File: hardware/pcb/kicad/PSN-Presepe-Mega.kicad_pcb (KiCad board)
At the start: 2 copper layers, 280 x 170 mm, 83 parts, among them J1 12V_IN, K1 G5Q-1_DC12, K10 G5Q-1_DC12, K11 G5Q-1_DC12, K12 G5Q-1_DC12, K13 G5Q-1_DC12, K14 G5Q-1_DC12, K15 G5Q-1_DC12, K16 G5Q-1_DC12, K2 G5Q-1_DC12, K3 G5Q-1_DC12, K4 G5Q-1_DC12, K5 G5Q-1_DC12, K6 G5Q-1_DC12, K7 G5Q-1_DC12, K8 G5Q-1_DC12, K9 G5Q-1_DC12, Q1 IRLZ44N_CIELO_R, Q2 IRLZ44N_CIELO_G, Q3 IRLZ44N_CIELO_B, Q4 IRLZ44N_TRAM_R, Q5 IRLZ44N_TRAM_G, Q6 IRLZ44N_TRAM_B, Q7 IRLZ44N_ALBA_R, Q8 IRLZ44N_ALBA_G, Q9 IRLZ44N_ALBA_B, U1 ULN2803C, U2 ULN2803C

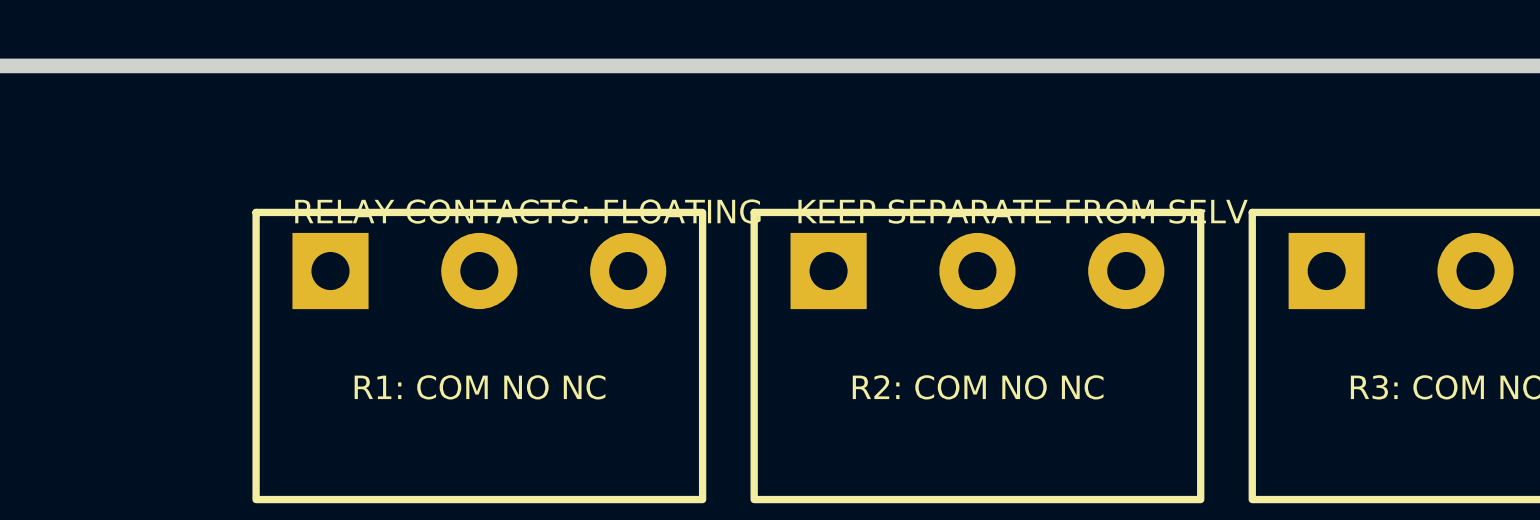
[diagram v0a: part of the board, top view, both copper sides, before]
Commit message: Remove redundant relay warning causing silk overlaps
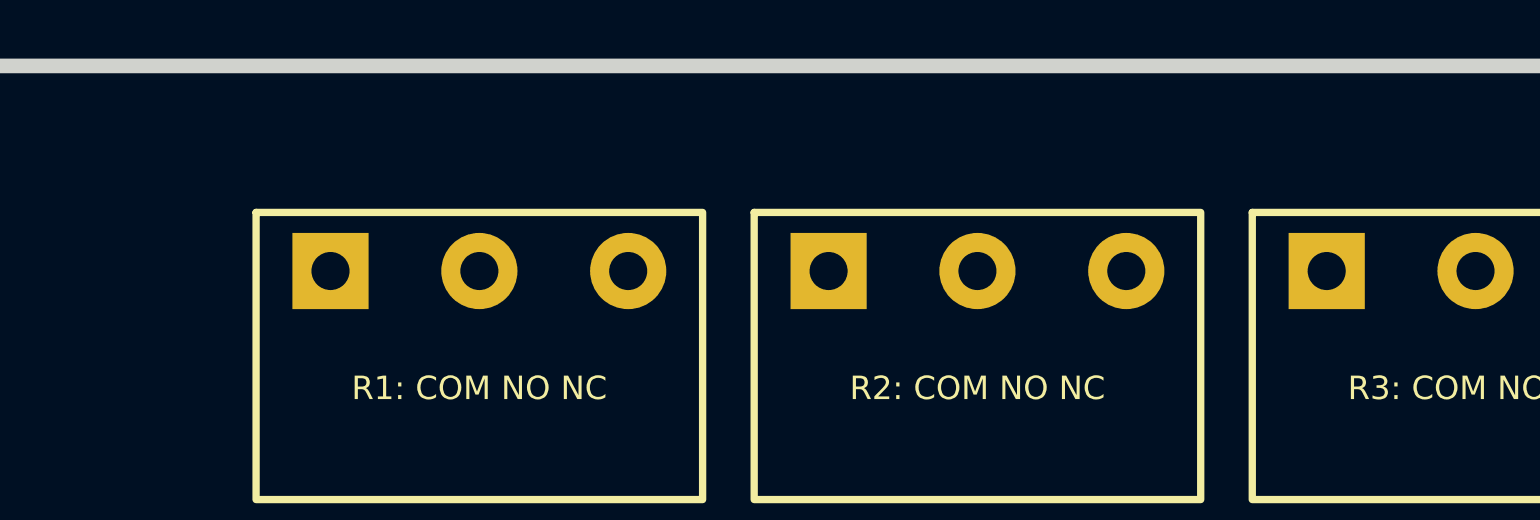
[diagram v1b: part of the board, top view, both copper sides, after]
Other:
- board text removed: "RELAY CONTACTS: FLOATING - KEEP SEPARATE FROM SELV"
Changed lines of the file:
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@@
   (gr_text "R15: COM NO NC" (at 286 149.08 90) (layer "F.SilkS") (effects (font (size 0.8 0.8) (thickness 0.12)) (justify)))
   (gr_text "R16: COM NO NC" (at 286 165.08 90) (layer "F.SilkS") (effects (font (size 0.8 0.8) (thickness 0.12)) (justify)))
-  (gr_text "RELAY CONTACTS: FLOATING - KEEP SEPARATE FROM SELV" (at 180 25) (layer "F.SilkS") (effects (font (size 0.8 0.8) (thickness 0.14))))
   (gr_text "NO GND PLANE UNDER CONTACT ROUTING" (at 100 35) (layer "F.SilkS") (effects (font (size 0.8 0.8) (thickness 0.12))))
   (footprint "MountingHole_1" (layer "F.Cu") (at 27 27)

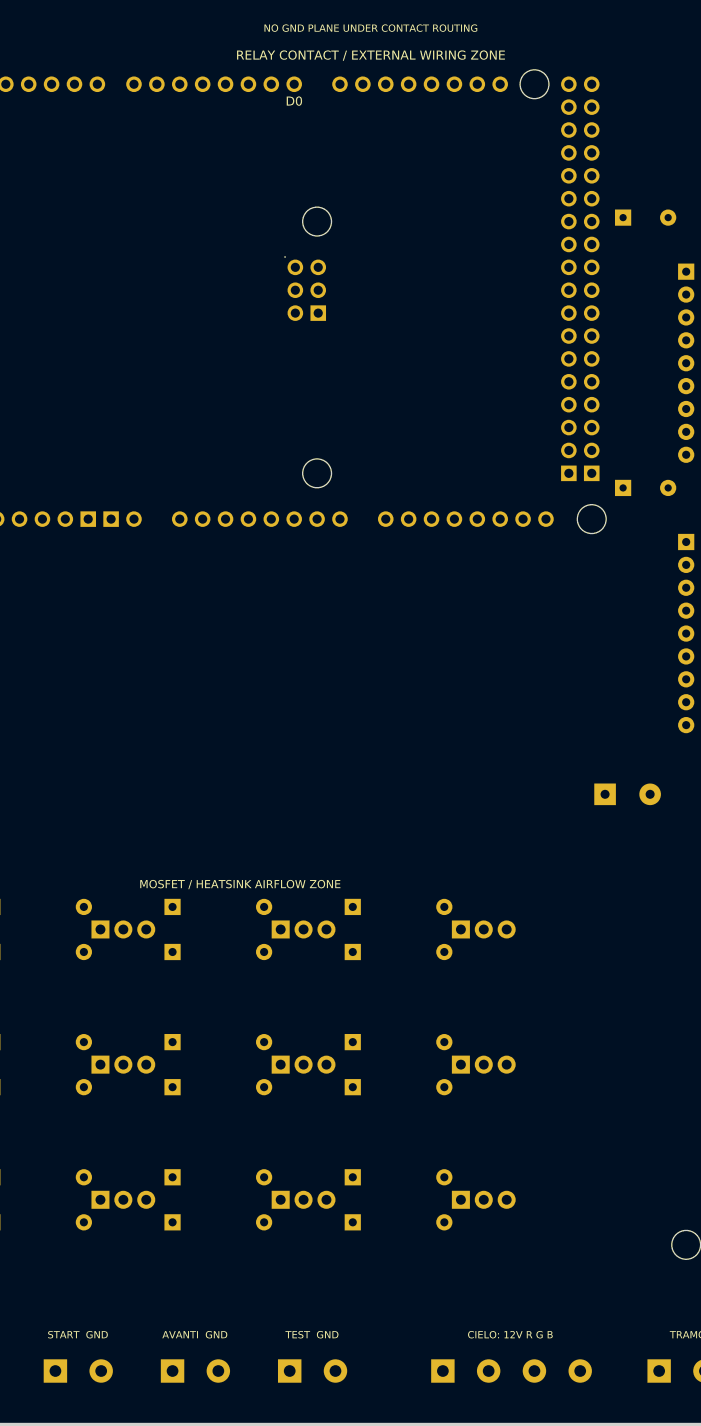
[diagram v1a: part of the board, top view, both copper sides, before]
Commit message: Promote first DRC-approved button routes
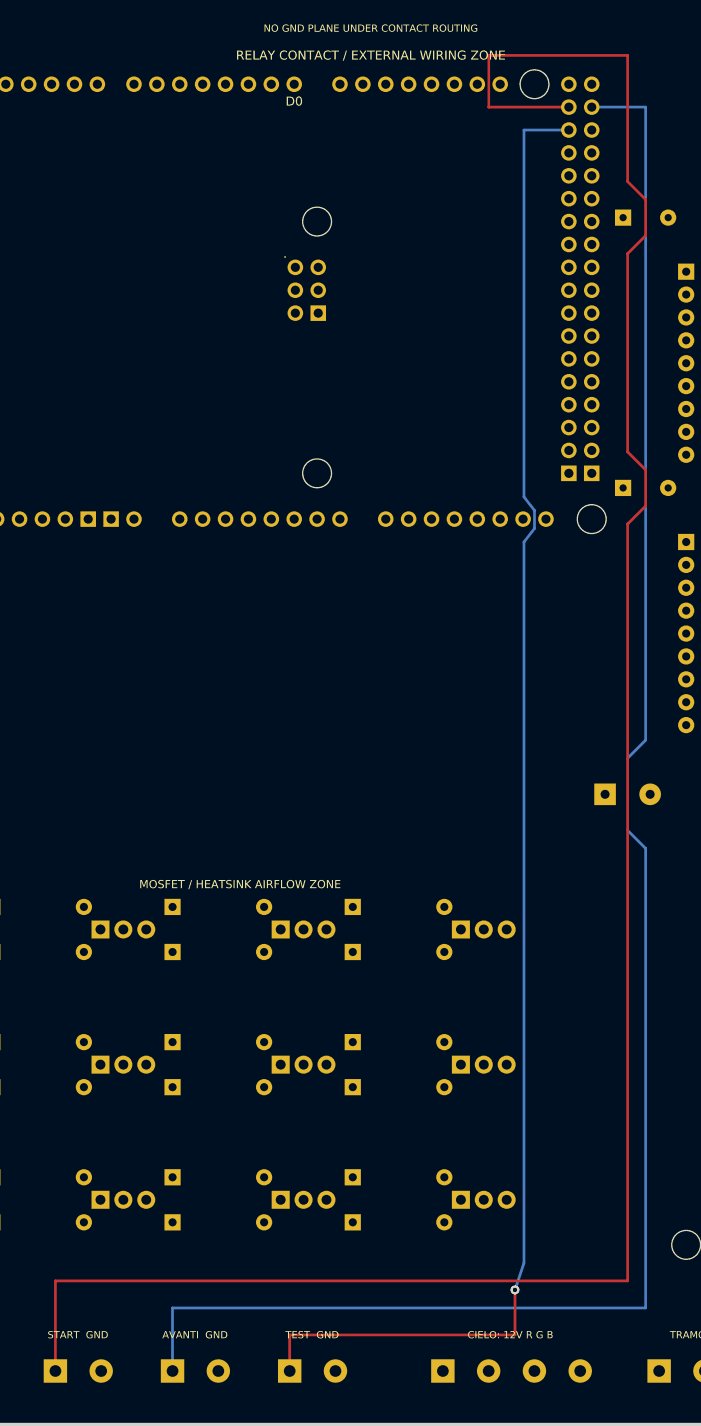
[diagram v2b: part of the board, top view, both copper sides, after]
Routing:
- net D22_START: track 0.00 -> 242.9 mm
- net D23_NEXT: track 0.00 -> 200.4 mm
- net D24_TEST: track 0.00 -> 168.7 mm, vias 0 -> 1
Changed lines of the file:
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@@
     (pad "VIN" thru_hole oval (at 45.72 -2.54) (size 1.7272 1.7272) (drill 1.016) (layers *.Cu *.Mask) (net 2 "+12V"))
   )
+  (segment (start 121.98 43.74) (end 113.09 43.74) (width 0.3) (layer "F.Cu") (net 16))
+  (segment (start 113.09 43.74) (end 113.09 38) (width 0.3) (layer "F.Cu") (net 16))
+  (segment (start 113.09 38) (end 128.5 38) (width 0.3) (layer "F.Cu") (net 16))
+  (segment (start 128.5 38) (end 128.5 52) (width 0.3) (layer "F.Cu") (net 16))
+  (segment (start 128.5 52) (end 130.5 54) (width 0.3) (layer "F.Cu") (net 16))
+  (segment (start 130.5 54) (end 130.5 58) (width 0.3) (layer "F.Cu") (net 16))
+  (segment (start 130.5 58) (end 128.5 60) (width 0.3) (layer "F.Cu") (net 16))
+  (segment (start 128.5 60) (end 128.5 82) (width 0.3) (layer "F.Cu") (net 16))
+  (segment (start 128.5 82) (end 130.5 84) (width 0.3) (layer "F.Cu") (net 16))
+  (segment (start 130.5 84) (end 130.5 88) (width 0.3) (layer "F.Cu") (net 16))
+  (segment (start 130.5 88) (end 128.5 90) (width 0.3) (layer "F.Cu") (net 16))
+  (segment (start 128.5 90) (end 128.5 174) (width 0.3) (layer "F.Cu") (net 16))
+  (segment (start 128.5 174) (end 65 174) (width 0.3) (layer "F.Cu") (net 16))
+  (segment (start 65 174) (end 65 184) (width 0.3) (layer "F.Cu") (net 16))
+  (segment (start 124.52 43.74) (end 130.5 43.74) (width 0.3) (layer "B.Cu") (net 17))
+  (segment (start 130.5 43.74) (end 130.5 114) (width 0.3) (layer "B.Cu") (net 17))
+  (segment (start 130.5 114) (end 128.5 116) (width 0.3) (layer "B.Cu") (net 17))
+  (segment (start 128.5 116) (end 128.5 124) (width 0.3) (layer "B.Cu") (net 17))
+  (segment (start 128.5 124) (end 130.5 126) (width 0.3) (layer "B.Cu") (net 17))
+  (segment (start 130.5 126) (end 130.5 177) (width 0.3) (layer "B.Cu") (net 17))
+  (segment (start 130.5 177) (end 78 177) (width 0.3) (layer "B.Cu") (net 17))
+  (segment (start 78 177) (end 78 184) (width 0.3) (layer "B.Cu") (net 17))
+  (segment (start 121.98 46.28) (end 117 46.28) (width 0.3) (layer "B.Cu") (net 18))
+  (segment (start 117 46.28) (end 117 87) (width 0.3) (layer "B.Cu") (net 18))
+  (segment (start 117 87) (end 118.17 88.5) (width 0.3) (layer "B.Cu") (net 18))
+  (segment (start 118.17 88.5) (end 118.17 90.5) (width 0.3) (layer "B.Cu") (net 18))
+  (segment (start 118.17 90.5) (end 117 92) (width 0.3) (layer "B.Cu") (net 18))
+  (segment (start 117 92) (end 117 172) (width 0.3) (layer "B.Cu") (net 18))
+  (segment (start 117 172) (end 116 175) (width 0.3) (layer "B.Cu") (net 18))
+  (segment (start 116 175) (end 116 180) (width 0.3) (layer "F.Cu") (net 18))
+  (segment (start 116 180) (end 91 180) (width 0.3) (layer "F.Cu") (net 18))
+  (segment (start 91 180) (end 91 184) (width 0.3) (layer "F.Cu") (net 18))
+  (via (at 116 175) (size 1.0) (drill 0.5) (layers "F.Cu" "B.Cu") (net 18))
   (gr_rect (start 20 20) (end 300 190) (stroke (width 0.5) (type default)) (fill none) (layer "Edge.Cuts"))
   (gr_rect (start 53 128) (end 118 172) (stroke (width 0.3) (type dash)) (fill none) (layer "Dwgs.User"))

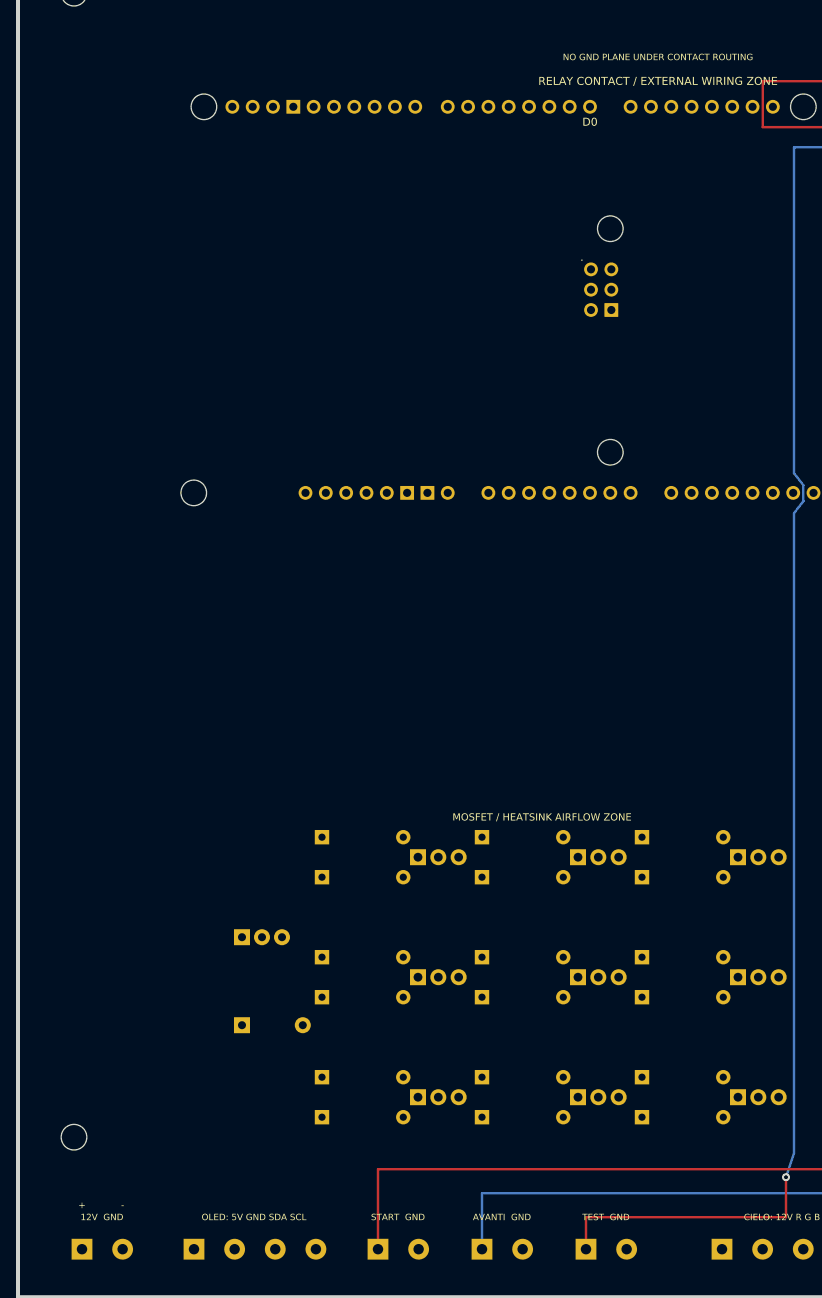
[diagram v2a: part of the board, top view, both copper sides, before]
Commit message: Promote DRC-clean OLED I2C routing
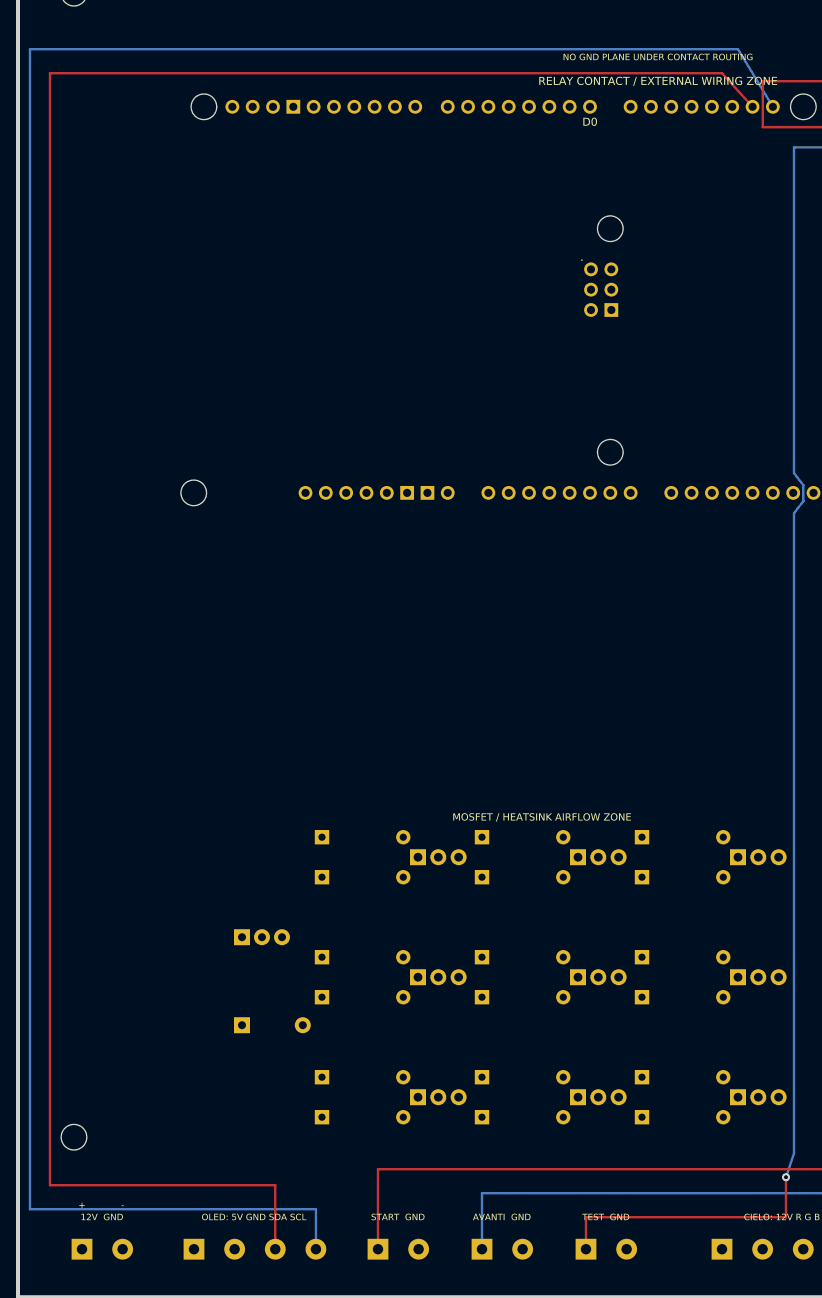
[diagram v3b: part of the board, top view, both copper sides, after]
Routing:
- net D21_SCL: track 0.00 -> 282.7 mm
- net D20_SDA: track 0.00 -> 264.8 mm
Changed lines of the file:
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@@
   (segment (start 91 180) (end 91 184) (width 0.3) (layer "F.Cu") (net 18))
   (via (at 116 175) (size 1.0) (drill 0.5) (layers "F.Cu" "B.Cu") (net 18))
+  (segment (start 111.82 41.2) (end 108 37) (width 0.3) (layer "F.Cu") (net 14))
+  (segment (start 108 37) (end 24 37) (width 0.3) (layer "F.Cu") (net 14))
+  (segment (start 24 37) (end 24 176) (width 0.3) (layer "F.Cu") (net 14))
+  (segment (start 24 176) (end 52.16 176) (width 0.3) (layer "F.Cu") (net 14))
+  (segment (start 52.16 176) (end 52.16 184) (width 0.3) (layer "F.Cu") (net 14))
+  (segment (start 114.36 41.2) (end 110 34) (width 0.3) (layer "B.Cu") (net 15))
+  (segment (start 110 34) (end 21.5 34) (width 0.3) (layer "B.Cu") (net 15))
+  (segment (start 21.5 34) (end 21.5 179) (width 0.3) (layer "B.Cu") (net 15))
+  (segment (start 21.5 179) (end 57.24 179) (width 0.3) (layer "B.Cu") (net 15))
+  (segment (start 57.24 179) (end 57.24 184) (width 0.3) (layer "B.Cu") (net 15))
   (gr_rect (start 20 20) (end 300 190) (stroke (width 0.5) (type default)) (fill none) (layer "Edge.Cuts"))
   (gr_rect (start 53 128) (end 118 172) (stroke (width 0.3) (type dash)) (fill none) (layer "Dwgs.User"))

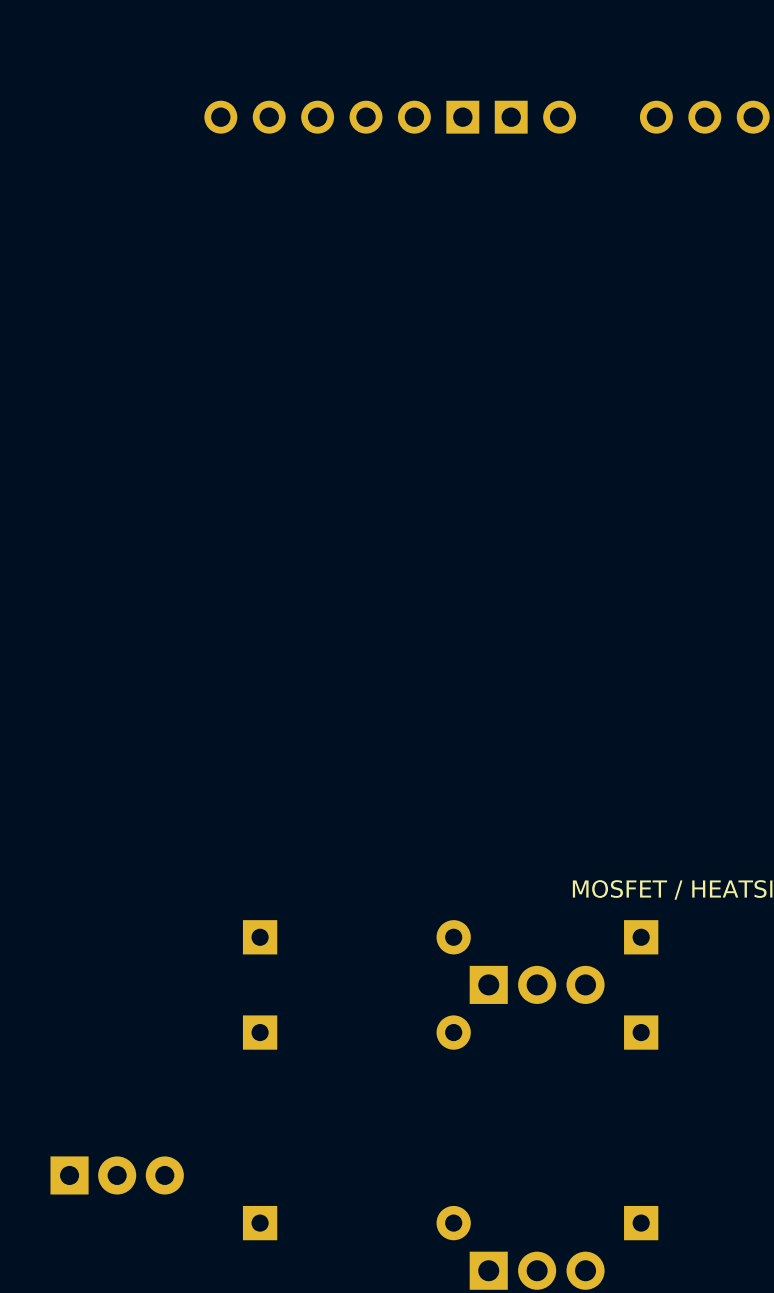
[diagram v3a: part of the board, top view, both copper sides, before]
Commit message: Promote clean A0 potentiometer routing
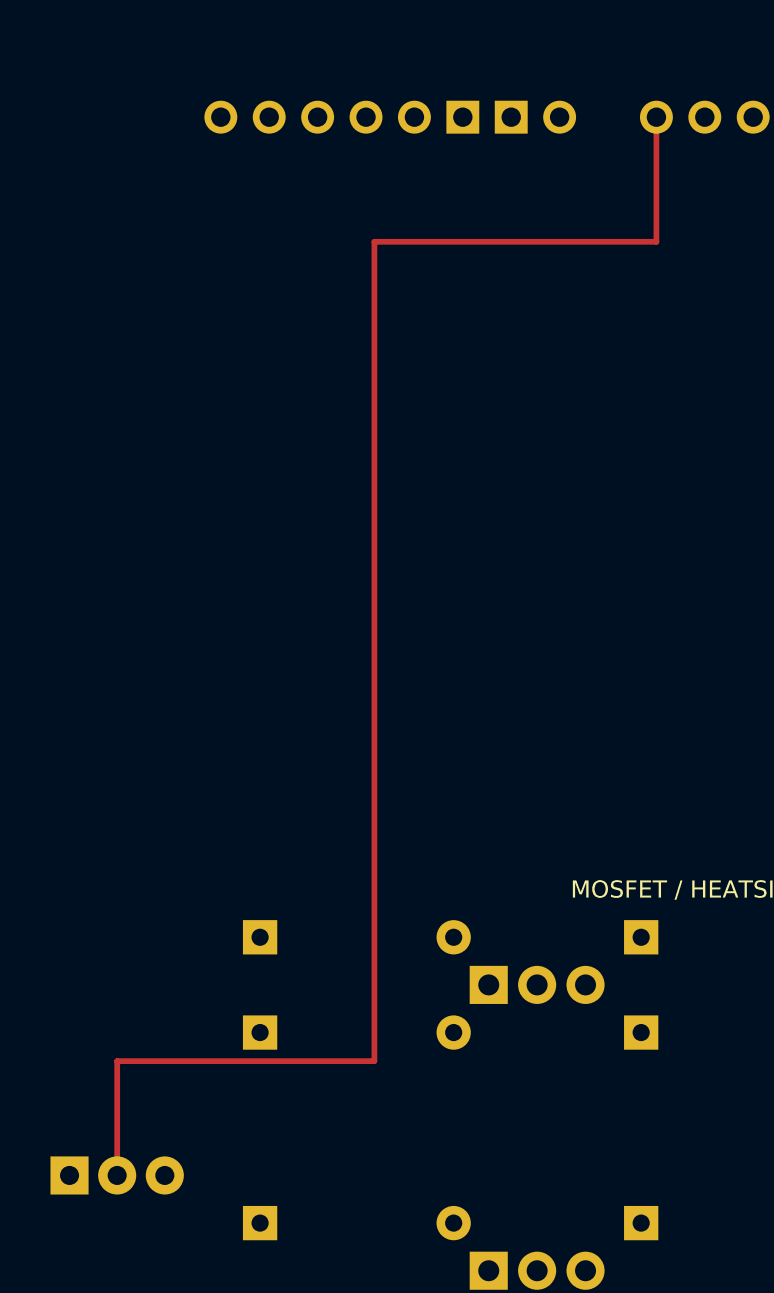
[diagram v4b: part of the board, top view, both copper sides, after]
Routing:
- net A0_POT: track 0.00 -> 83.8 mm
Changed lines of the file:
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@@
   (segment (start 21.5 179) (end 57.24 179) (width 0.3) (layer "B.Cu") (net 15))
   (segment (start 57.24 179) (end 57.24 184) (width 0.3) (layer "B.Cu") (net 15))
+  (segment (start 78.8 89.46) (end 78.8 96) (width 0.3) (layer "F.Cu") (net 19))
+  (segment (start 78.8 96) (end 64 96) (width 0.3) (layer "F.Cu") (net 19))
+  (segment (start 64 96) (end 64 139) (width 0.3) (layer "F.Cu") (net 19))
+  (segment (start 64 139) (end 50.5 139) (width 0.3) (layer "F.Cu") (net 19))
+  (segment (start 50.5 139) (end 50.5 145) (width 0.3) (layer "F.Cu") (net 19))
   (gr_rect (start 20 20) (end 300 190) (stroke (width 0.5) (type default)) (fill none) (layer "Edge.Cuts"))
   (gr_rect (start 53 128) (end 118 172) (stroke (width 0.3) (type dash)) (fill none) (layer "Dwgs.User"))
